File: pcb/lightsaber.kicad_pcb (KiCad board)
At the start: 4 copper layers, 100 x 28 mm, 62 parts, among them IC1 BMI055, J1 2012670005, J2 Screw_Terminal_01x05, J3 ESP32 Prog, J4 ESP32 JTAG, J5 Conn_01x02, J6 Conn_01x06, Q1 PMOS, Q2 NPN, SW1 SW_Push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

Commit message: Tidying up routing
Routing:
- net ESP_LED_DEBUG: track 57.5 -> 59.1 mm
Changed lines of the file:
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@@
   (via (at 130.015 86.5) (size 0.45) (drill 0.3) (layers "F.Cu" "B.Cu") (net 12))
   (segment (start 128.35 85.25) (end 129.6 86.5) (width 0.2) (layer "B.Cu") (net 12))
-  (segment (start 172.25 74.6) (end 177.05 79.4) (width 0.2) (layer "B.Cu") (net 12))
+  (segment (start 144.7 74.6) (end 172.5 74.6) (width 0.2) (layer "B.Cu") (net 12))
+  (segment (start 177.3 79.4) (end 178.15 79.4) (width 0.2) (layer "B.Cu") (net 12))
   (segment (start 132.815 86.5) (end 130.015 86.5) (width 0.2) (layer "B.Cu") (net 12))
+  (segment (start 172.5 74.6) (end 177.3 79.4) (width 0.2) (layer "B.Cu") (net 12))
   (segment (start 129.6 86.5) (end 130.015 86.5) (width 0.2) (layer "B.Cu") (net 12))
-  (segment (start 177.05 79.4) (end 178.15 79.4) (width 0.2) (layer "B.Cu") (net 12))
   (segment (start 135.115 84.2) (end 132.815 86.5) (width 0.2) (layer "B.Cu") (net 12))
-  (segment (start 144.7 74.6) (end 172.25 74.6) (width 0.2) (layer "B.Cu") (net 12))
   (segment (start 129.2 85) (end 129.715 85) (width 0.2) (layer "F.Cu") (net 13))
   (segment (start 131.64 82.65) (end 131.59 82.6) (width 0.2) (layer "F.Cu") (net 13))
@@
   (segment (start 157.1125 84.05) (end 157.17 84.1075) (width 0.6) (layer "F.Cu") (net 15))
   (segment (start 155.22 84.05) (end 157.1125 84.05) (width 0.6) (layer "F.Cu") (net 15))
-  (segment (start 179.12 85.68) (end 180.15 85.68) (width 0.2) (layer "F.Cu") (net 17))
-  (segment (start 175.3 89.5) (end 179.12 85.68) (width 0.2) (layer "F.Cu") (net 17))
-  (segment (start 164.15 87.55) (end 166.1 89.5) (width 0.2) (layer "F.Cu") (net 17))
-  (segment (start 166.1 89.5) (end 175.3 89.5) (width 0.2) (layer "F.Cu") (net 17))
+  (segment (start 168 91.4) (end 173.7 91.4) (width 0.2) (layer "F.Cu") (net 17))
+  (segment (start 179.42 85.68) (end 180.15 85.68) (width 0.2) (layer "F.Cu") (net 17))
+  (segment (start 164.15 87.55) (end 168 91.4) (width 0.2) (layer "F.Cu") (net 17))
+  (segment (start 173.7 91.4) (end 179.42 85.68) (width 0.2) (layer "F.Cu") (net 17))
   (via (at 164.15 87.55) (size 0.45) (drill 0.3) (layers "F.Cu" "B.Cu") (net 17))
   (segment (start 150.6 88.25) (end 151.3 88.95) (width 0.2) (layer "B.Cu") (net 17))
@@
   (via (at 160.85 84.4) (size 0.45) (drill 0.3) (layers "F.Cu" "B.Cu") (net 31))
   (via (at 140.25 77.2) (size 0.45) (drill 0.3) (layers "F.Cu" "B.Cu") (net 31))
-  (segment (start 132.95 78.75) (end 134.5 77.2) (width 0.2) (layer "B.Cu") (net 31))
   (segment (start 140.25 77.2) (end 148.8 77.2) (width 0.2) (layer "B.Cu") (net 31))
-  (segment (start 134.5 77.2) (end 136.1 77.2) (width 0.2) (layer "B.Cu") (net 31))
+  (segment (start 148.8 77.2) (end 151.55 79.95) (width 0.2) (layer "B.Cu") (net 31))
+  (segment (start 134.55 78.75) (end 136.1 77.2) (width 0.2) (layer "B.Cu") (net 31))
   (segment (start 129.25 78) (end 130 78.75) (width 0.2) (layer "B.Cu") (net 31))
-  (segment (start 130 78.75) (end 132.95 78.75) (width 0.2) (layer "B.Cu") (net 31))
-  (segment (start 148.8 77.2) (end 151.55 79.95) (width 0.2) (layer "B.Cu") (net 31))
   (segment (start 151.55 79.95) (end 156 84.4) (width 0.2) (layer "B.Cu") (net 31))
+  (segment (start 130 78.75) (end 134.55 78.75) (width 0.2) (layer "B.Cu") (net 31))
   (segment (start 156 84.4) (end 160.85 84.4) (width 0.2) (layer "B.Cu") (net 31))
   (segment (start 130.53 74.82) (end 130.55 74.8) (width 0.2) (layer "F.Cu") (net 32))
@@
   (via (at 160.85 85.7) (size 0.45) (drill 0.3) (layers "F.Cu" "B.Cu") (net 32))
   (via (at 130.55 74.8) (size 0.45) (drill 0.3) (layers "F.Cu" "B.Cu") (net 32))
+  (segment (start 156 85.7) (end 160.85 85.7) (width 0.2) (layer "B.Cu") (net 32))
+  (segment (start 136.0547 74.5547) (end 139.35 77.85) (width 0.2) (layer "B.Cu") (net 32))
+  (segment (start 130.7953 74.5547) (end 136.0547 74.5547) (width 0.2) (layer "B.Cu") (net 32))
+  (segment (start 139.35 77.85) (end 148.15 77.85) (width 0.2) (layer "B.Cu") (net 32))
+  (segment (start 148.15 77.85) (end 156 85.7) (width 0.2) (layer "B.Cu") (net 32))
   (segment (start 130.55 74.8) (end 130.7953 74.5547) (width 0.2) (layer "B.Cu") (net 32))
-  (segment (start 139.8 77.85) (end 148.15 77.85) (width 0.2) (layer "B.Cu") (net 32))
-  (segment (start 148.15 77.85) (end 156 85.7) (width 0.2) (layer "B.Cu") (net 32))
-  (segment (start 130.7953 74.5547) (end 136.5047 74.5547) (width 0.2) (layer "B.Cu") (net 32))
-  (segment (start 156 85.7) (end 160.85 85.7) (width 0.2) (layer "B.Cu") (net 32))
-  (segment (start 136.5047 74.5547) (end 139.8 77.85) (width 0.2) (layer "B.Cu") (net 32))
   (segment (start 127.99 74.81) (end 128.9 73.9) (width 0.2) (layer "F.Cu") (net 33))
   (segment (start 136.1 75.6) (end 134.4 73.9) (width 0.2) (layer "F.Cu") (net 33))
@@
         (xy 217 93.05)
         (xy 207.95 93.8)
-        (xy 207.95 93.8)
         (xy 206 93.8)

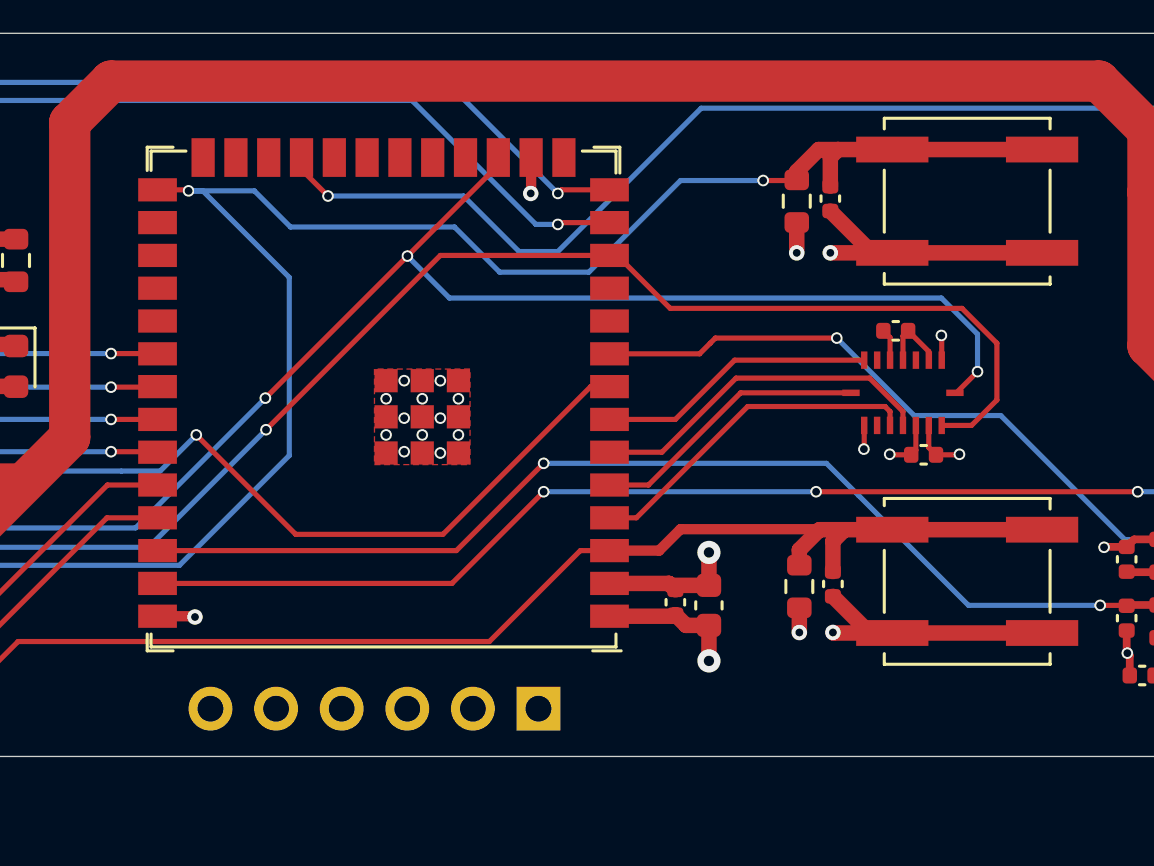
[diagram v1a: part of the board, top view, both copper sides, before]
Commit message: Adding external IO
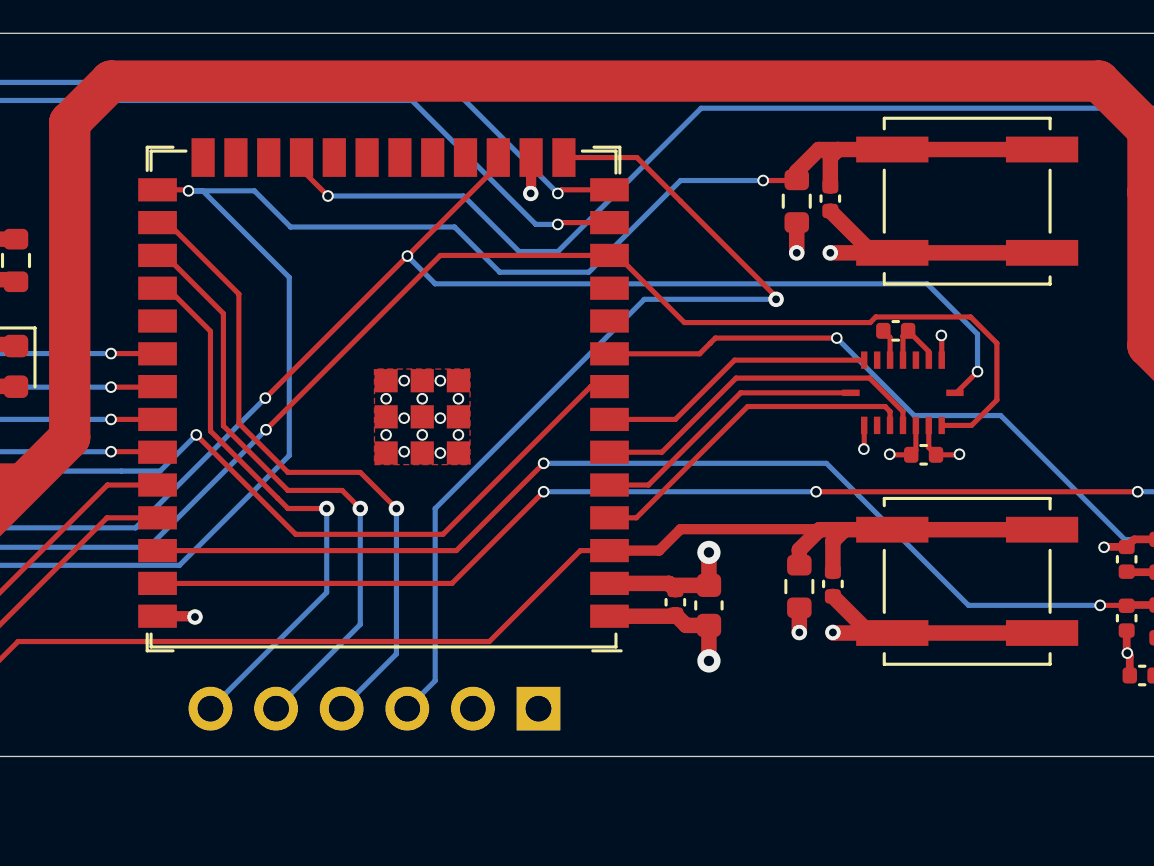
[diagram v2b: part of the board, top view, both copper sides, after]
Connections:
- J6 pad 1: unconnected-(J6-Pin_1-Pad1) -> +3.3V
- J6 pad 2: unconnected-(J6-Pin_2-Pad2) -> GND
- J6 pad 3: unconnected-(J6-Pin_3-Pad3) -> ESP32_EXTERN_ADC
- J6 pad 4: unconnected-(J6-Pin_4-Pad4) -> ESP32_EXTERN_IO35
- J6 pad 5: unconnected-(J6-Pin_5-Pad5) -> ESP32_EXTERN_IO36
- J6 pad 6: unconnected-(J6-Pin_6-Pad6) -> ESP32_EXTERN_IO37
- U2 pad 15: unconnected-(U2-GPIO3/TOUCH3/ADC1_CH2-Pad15) -> ESP32_EXTERN_ADC
- U2 pad 28: unconnected-(U2-SPIIO6/GPIO35/FSPID/SUBSPID-Pad28) -> ESP32_EXTERN_IO35
- U2 pad 29: unconnected-(U2-SPIIO7/GPIO36/FSPICLK/SUBSPICLK-Pad29) -> ESP32_EXTERN_IO36
- U2 pad 30: unconnected-(U2-SPIDQS/GPIO37/FSPIQ/SUBSPIQ-Pad30) -> ESP32_EXTERN_IO37
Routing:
- net ESP32_EXTERN_ADC: track 0.00 -> 35.3 mm, vias 0 -> 1
- net ESP32_EXTERN_IO35: track 0.00 -> 25.4 mm, vias 0 -> 1
- net ESP32_EXTERN_IO36: track 0.00 -> 23.6 mm, vias 0 -> 1
- net ESP32_EXTERN_IO37: track 0.00 -> 22.0 mm, vias 0 -> 1

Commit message: Tidying up traces
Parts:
- J6: value Conn_01x06 -> Conn_01x10; footprint Connector_PinHeader_2.54mm:PinHeader_1x06_P2.54mm_Vertical -> Connector_PinHeader_2.54mm:PinHeader_1x10_P2.54mm_Vertical; moved to F.Cu
- moved J6 2.68 mm to (180.1, 98.2), turned to -90 degrees
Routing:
- net ESP32_I2C_SCL: track 62.7 -> 71.7 mm, vias 4 -> 6
- net ESP32_I2C_SDA: track 60.6 -> 68.8 mm, vias 2 -> 4
- net D-: track 62.3 -> 63.7 mm
- net ESP_IO0: track 95.1 -> 93.9 mm
- net ESP32_EXTERN_IO37: track 22.0 -> 20.9 mm
- net ESP32_EXTERN_IO36: track 23.6 -> 22.5 mm
- net ESP_UART_RX: track 39.9 -> 40.8 mm
- net ESP_UART_TX: track 41.3 -> 42.0 mm
- net ESP32_EXTERN_IO35: track 25.4 -> 24.8 mm
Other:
- board text added: "3V3 GND ADC2 IO35 IO36 IO37 SCL SDA GND 3V3"
